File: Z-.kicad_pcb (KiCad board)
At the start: 4 copper layers, 98 x 98 mm, 147 parts, among them J1 200528-0100, J2 U.FL, J3 U.FL, J5 Conn_01x02, Q1 NX3008NBKS, Q10 MBT2222ADW1T1, Q11 NX3008NBKS, Q12 MBT2222ADW1T1, Q13 IRLML2803, Q14 SiRA99DP, Q15 IRFTS9342PBF, Q17 IRFTS9342PBF, Q19 IRFTS9342PBF, Q2 MBT2222ADW1T1, Q20 IRLML2803, Q21 SiRA99DP, Q3 NX3008NBKS, Q4 MBT2222ADW1T1, Q5 NX3008NBKS, Q6 MBT2222ADW1T1, Q7 NX3008NBKS, Q8 MBT2222ADW1T1, Q9 NX3008NBKS, U1 OPT4003DNPRQ1, U2 PCA9633DP2, U4 DRV8235RTER, U5 USBLC6-2P6

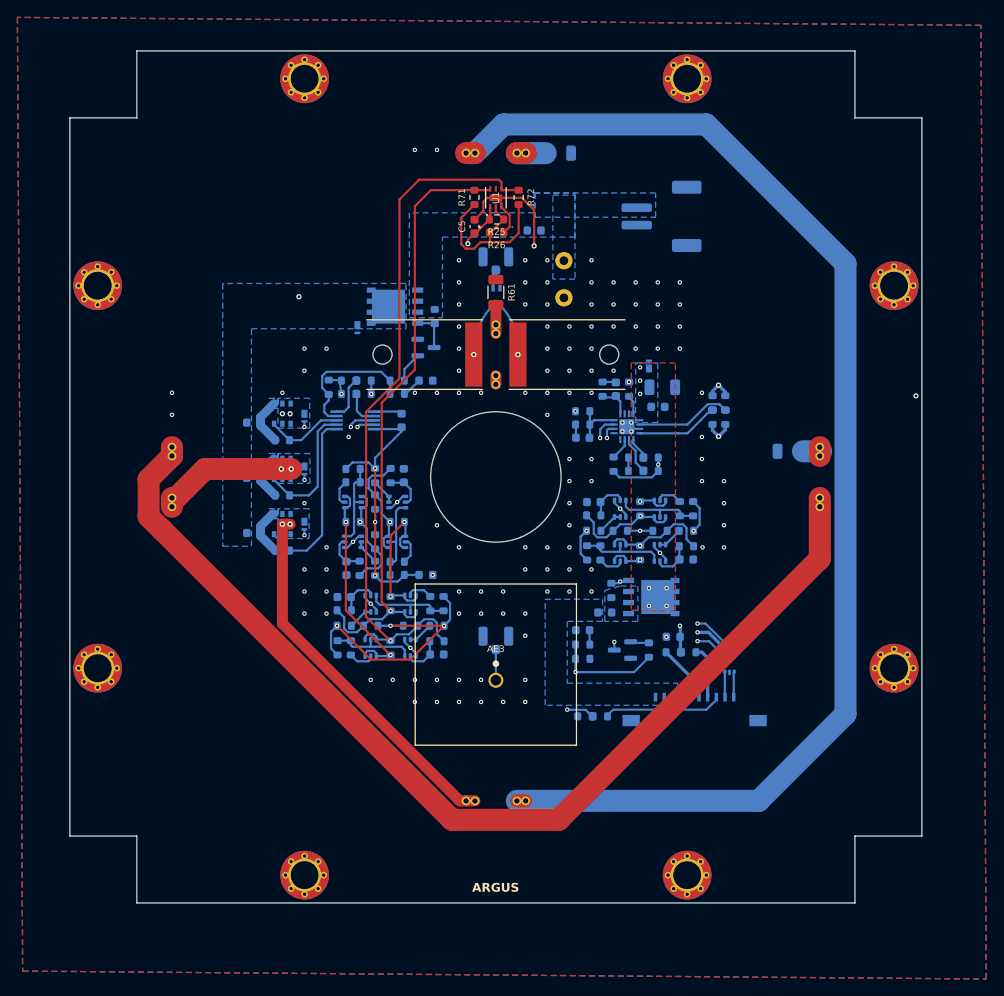
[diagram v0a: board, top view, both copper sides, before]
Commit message: Updated burnwire footprint and fuse specs
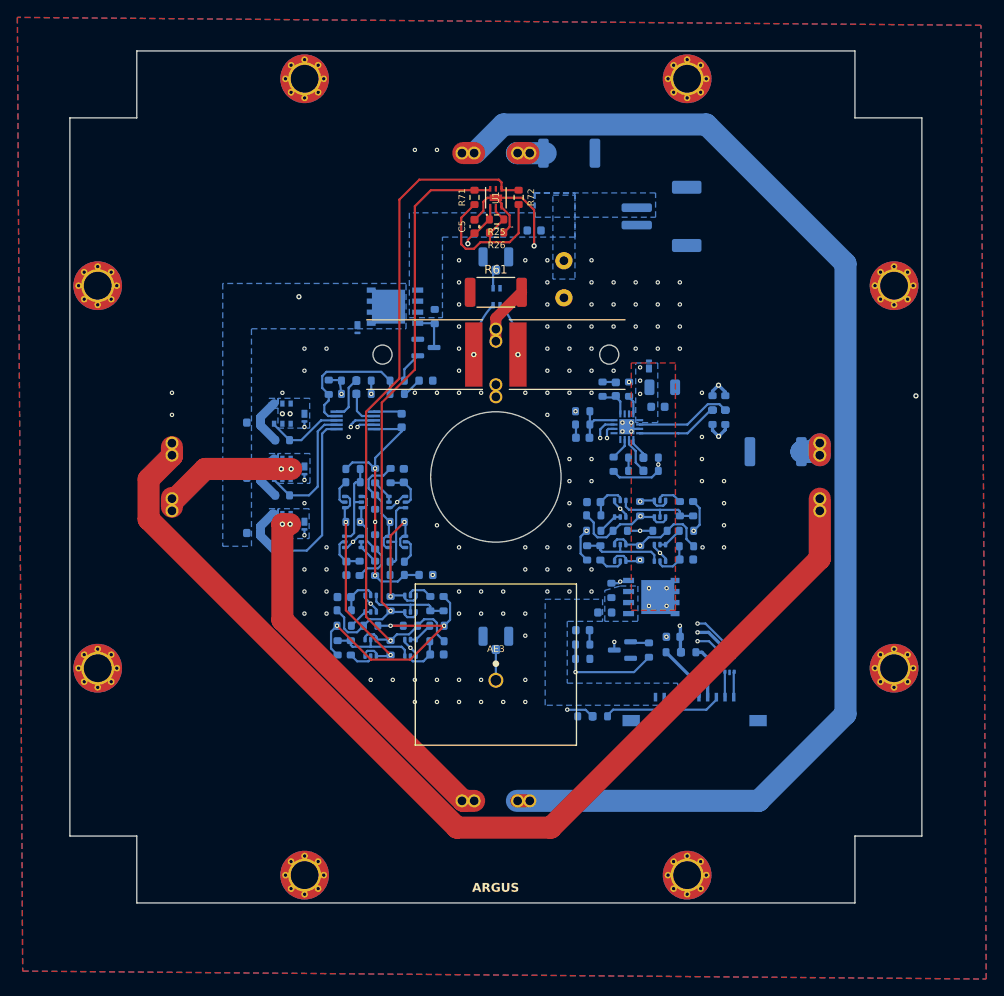
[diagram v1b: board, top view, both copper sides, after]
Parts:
- R43, R53, R60: value 100K -> 1k
- R44, R55, R61: footprint Resistor_SMD:R_1206_3216Metric -> Resistor_SMD:R_2512_6332Metric
- moved R44 1.68 mm to (184.5, 92.8)
- moved R55 1.24 mm to (160.8, 58.4)
- moved JP3 0.97 mm to (152.3, 82.5)
- turned R61 to 0 degrees
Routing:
- net Net-(JP3-B): track 3.29 -> 6.86 mm
- net Net-(JP4-B): track 3.11 -> 6.00 mm
- net /Burn Wires/VBURN3: track 28.1 -> 26.3 mm
- net Net-(JP1-B): track 120.2 -> 121.0 mm
- net /Burn Wires/VBURN2: track 42.9 -> 43.6 mm
- net GND: vias 130 -> 128

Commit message: Minor layout tweaks and gerbers exported
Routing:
- net GND: vias 128 -> 130
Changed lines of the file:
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@@
 			(drillshape 0)
 			(scaleselection 1)
-			(outputdirectory "../../../Gerbers/")
+			(outputdirectory "./Gerber")
 		)
 	)
@@
 			(pinfunction "MountPin")
 			(pintype "passive")
+			(zone_connect 1)
 		)
 		(pad "MP" smd rect
@@
 			(pinfunction "MountPin")
 			(pintype "passive")
+			(zone_connect 1)
 		)
 		(model "${KIPRJMOD}/../KiCad-Libraries/3D Models/2005280100.stp"
@@
 	)
 	(via
+		(at 172.72 117.856)
+		(size 0.508)
+		(drill 0.254)
+		(layers "F.Cu" "B.Cu")
+		(free yes)
+		(net 1)
+	)
+	(via
 		(at 163.322 106.299)
 		(size 0.508)
@@
 		(net 1)
 	)
+	(via
+		(at 172.212 118.618)
+		(size 0.508)
+		(drill 0.254)
+		(layers "F.Cu" "B.Cu")
+		(free yes)
+		(net 1)
+	)

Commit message: push
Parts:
- removed D8: GREEN, LED_SMD:LED_0603_1608Metric
- removed Q14: SiRA99DP, Argus-Miscellaneous:PowerPAK SO-8
- removed R73: 10k, Resistor_SMD:R_0603_1608Metric
- removed U5: USBLC6-2P6, Package_TO_SOT_SMD:SOT-666
- added D1: 10V, Diode_SMD:Nexperia_DSN1608-2_1.6x0.8mm, B.Cu at (154.7, 75.4)
- added F8: 1A, Fuse:Fuse_0603_1608Metric, B.Cu at (177.3, 73.2)
- added K1: G6B-1114P-US DC6, Argus-Miscellaneous:RELAY_G6B-1114P-US_OMR, B.Cu at (156.8, 73.2)
- added U3: USBLC6-2P6, Package_TO_SOT_SMD:SOT-666, B.Cu at (168.9, 118.4)
- AE1, AE2: footprint Argus-Miscellaneous:Antenna Mount -> Argus-Miscellaneous:Antenna Mount v2; moved to B.Cu
- D7: value 10V -> GREEN; footprint Diode_SMD:Nexperia_DSN1608-2_1.6x0.8mm -> LED_SMD:LED_0603_1608Metric
- F4, F5, F6: value 500mA -> 2A
- F7: value 2A -> 5A
- R61: moved to B.Cu
- moved R81 45.5 mm to (143.5, 82.5), turned to -90 degrees
- moved R80 43.0 mm to (143.5, 84.3), turned to 90 degrees
- moved R69 39.1 mm to (172.2, 86.9), turned to 180 degrees
- moved D5 36.5 mm to (147.8, 69.1), turned to 180 degrees
- moved F2 36.0 mm to (133.3, 72.6), turned to 90 degrees
- moved R53 35.8 mm to (147.8, 74.4)
- moved Q17 35.6 mm to (147.8, 71.6), turned to 180 degrees
- moved F5 34.9 mm to (147.8, 76.2), turned to 0 degrees
- moved D7 31.8 mm to (167.6, 84.3)
- moved R61 31.5 mm to (152.4, 105.9), turned to 90 degrees
- moved F4 30.4 mm to (151.9, 76.2), turned to 0 degrees
- moved R70 30.2 mm to (171.2, 84.3), turned to 90 degrees
- moved Q13 30.1 mm to (174.2, 84.3)
- moved R60 29.5 mm to (151.9, 74.4)
- moved Q19 29.4 mm to (151.9, 71.6), turned to 180 degrees
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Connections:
- D7 pad 1: /Burn Wires/VBURN_A_IN -> GND
- D7 pad 2: GND -> Net-(D7-A)
- F4 pad 2: /Burn Wires/VBURN_A_IN -> Net-(D1-K)
- F5 pad 2: /Burn Wires/VBURN_A_IN -> Net-(D1-K)
- F6 pad 2: /Burn Wires/VBURN_A_IN -> Net-(D1-K)
- R68 pad 2: Net-(D8-A) -> Net-(D7-A)
- U2 pad 1: BURN_EN2 -> BURN_EN1
- U2 pad 2: BURN_EN1 -> BURN_EN2
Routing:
- net Net-(JP2-B): track 146.6 -> 1.02 mm
- net Net-(JP1-B): track 121.0 -> 0.00 mm
- net LS_3V3: track 113.1 -> 16.0 mm, vias 5 -> 4
- net SDA: track 88.4 -> 11.8 mm, vias 4 -> 0
- net SCL: track 83.3 -> 11.8 mm, vias 4 -> 0
- net MAIN_3V3: track 84.7 -> 13.9 mm, vias 7 -> 3
- net SCL_LS: track 82.0 -> 12.5 mm, vias 1 -> 0
- net PERI_3V3: track 59.2 -> 0.00 mm, vias 3 -> 0
- net SDA_LS: track 70.9 -> 12.3 mm, vias 1 -> 0
- net /Burn Wires/VBURN2: track 43.6 -> 1.02 mm
- net /Burn Wires/VBURN3: track 26.3 -> 0.00 mm
- net BW_3V3: track 34.1 -> 10.8 mm
- net GND: track 47.9 -> 25.9 mm, vias 130 -> 9
- net BURN_RELAY_A: track 16.2 -> 35.5 mm, vias 0 -> 2
- net SCL_M: track 29.9 -> 11.8 mm, vias 2 -> 1
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- added copper zone on B.Cu, net Net-(D1-K)
- removed copper zone on B.Cu, net /Burn Wires/VBURN_A_IN
- removed copper zone on B.Cu, net /I2C Devices/VM
- removed copper zone on F.Cu, net /I2C Devices/VM
- removed copper zone on B.Cu, net GND
- removed copper zone on F.Cu, net GND
- removed copper zone on In1.Cu, net GND
- removed copper zone on In2.Cu, net GND
- removed copper zone on B.Cu, net Net-(F7-Pad1)
- removed copper zone on B.Cu, net Net-(Q21-S)
- removed copper zone on B.Cu, net VBATT
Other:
- outline, holes or cut-outs redrawn

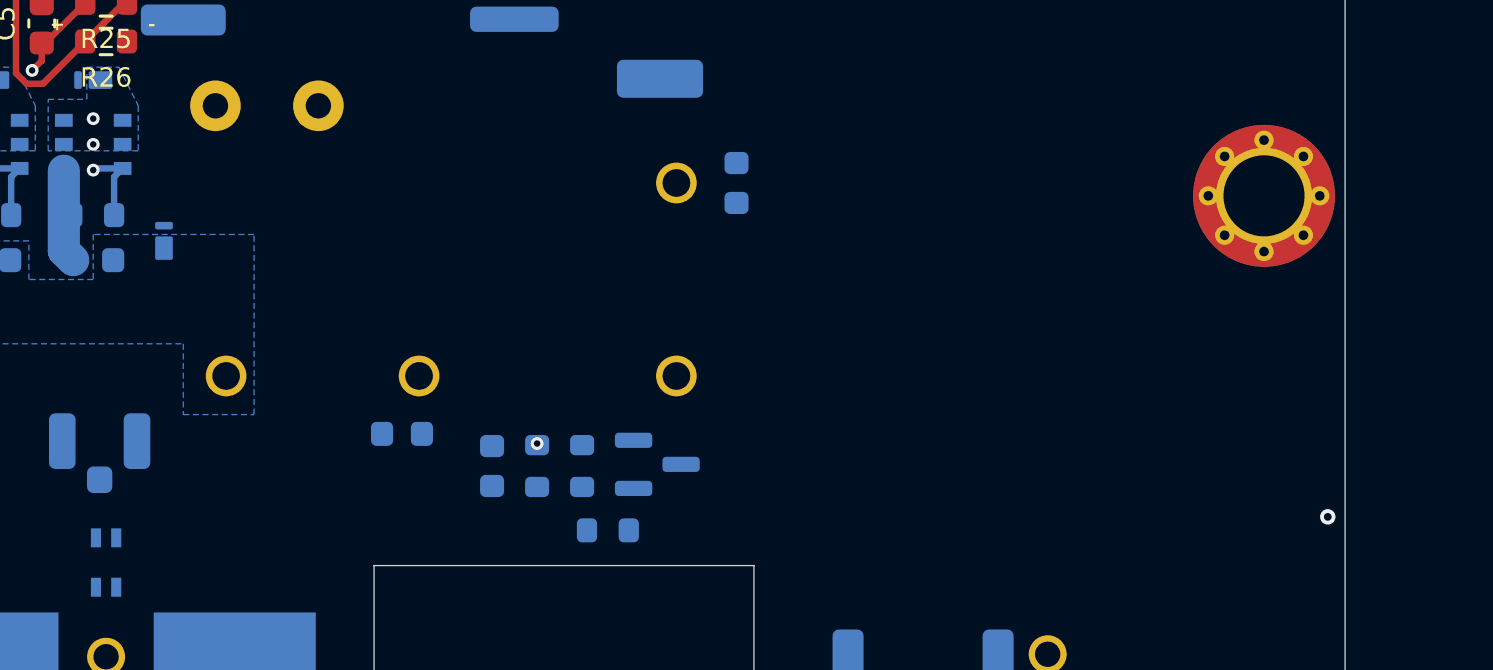
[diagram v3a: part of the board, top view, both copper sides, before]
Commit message: updated relay with old relay
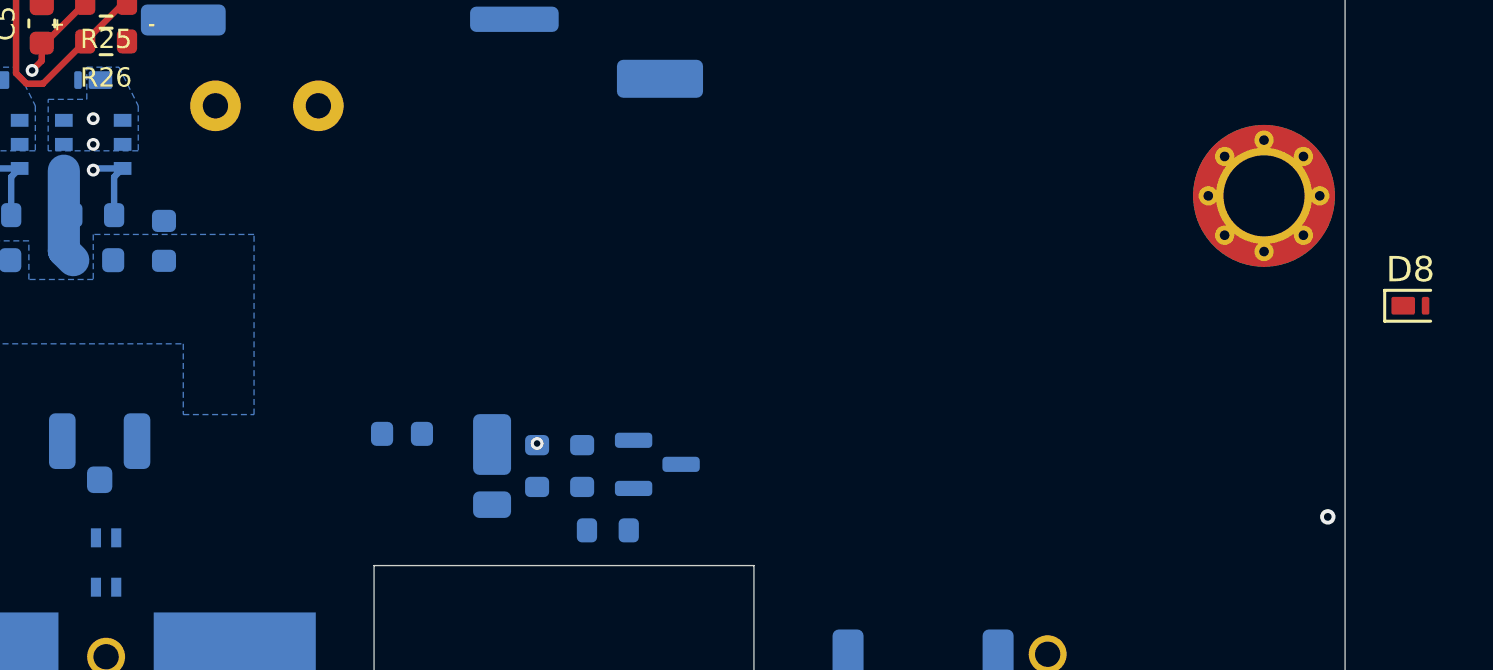
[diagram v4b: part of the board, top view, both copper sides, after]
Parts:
- removed F8: 1A, Fuse:Fuse_0603_1608Metric
- removed K1: G6B-1114P-US DC6, Argus-Miscellaneous:RELAY_G6B-1114P-US_OMR
- added D8: 10V, Diode_SMD:Nexperia_DSN1608-2_1.6x0.8mm, F.Cu at (203.9, 78.0)
- D1: value 10V -> GREEN; footprint Diode_SMD:Nexperia_DSN1608-2_1.6x0.8mm -> LED_SMD:LED_0603_1608Metric
- D7: value GREEN -> DFLS130L; footprint LED_SMD:LED_0603_1608Metric -> Diode_SMD:D_PowerDI-123
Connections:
- D1 pad 1: Net-(D1-K) -> GND
- D1 pad 2: GND -> Net-(D1-A)
- D7 pad 1: GND -> Net-(D7-K)
- F4 pad 2: Net-(D1-K) -> /Burn Wires/VBURN_A_IN
- F5 pad 2: Net-(D1-K) -> /Burn Wires/VBURN_A_IN
- F6 pad 2: Net-(D1-K) -> /Burn Wires/VBURN_A_IN
- F7 pad 1: Net-(F7-Pad1) -> Net-(D7-K)
- Q13 pad 3: Net-(Q13-D) -> Net-(D7-A)
- R68 pad 2: Net-(D7-A) -> Net-(D1-A)
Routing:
- added copper zone on B.Cu, net /Burn Wires/VBURN_A_IN
- removed copper zone on B.Cu, net Net-(D1-K)

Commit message: Updated PCB
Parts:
- added K1: IM02, Argus-Miscellaneous:RELAY8_SMTGUL_TEC, B.Cu at (163.3, 79.0)
- D8: moved to B.Cu
- moved JP2 74.5 mm to (152.4, 58.4)
- moved JP5 74.4 mm to (152.4, 132.8), turned to -90 degrees
- moved R55 64.1 mm to (149.1, 127.5), turned to -90 degrees
- moved D8 43.6 mm to (160.8, 84.3), turned to 180 degrees
- moved R80 34.7 mm to (146.3, 118.9)
- moved R81 34.7 mm to (146.3, 117.1)
- moved D1 20.7 mm to (174.2, 82.3), turned to 180 degrees
- moved D7 11.7 mm to (165.4, 72.9), turned to 0 degrees
- moved F7 10.7 mm to (160.8, 72.9)
- moved R69 8.38 mm to (174.2, 78.7), turned to -90 degrees
- moved Q13 8.20 mm to (171.4, 76.5), turned to 90 degrees
- moved R70 4.32 mm to (171.2, 80.0), turned to 180 degrees
- moved R68 2.70 mm to (171.2, 82.3), turned to 0 degrees
- moved F3 1.80 mm to (146.3, 113.8), turned to 90 degrees
- moved H10 1.52 mm to (162.3, 70.1)
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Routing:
- net Net-(JP2-B): track 1.02 -> 116.3 mm
- net Net-(JP1-B): track 0.00 -> 88.7 mm
- net SDA: track 11.8 -> 98.9 mm, vias 0 -> 4
- net SCL: track 11.8 -> 89.2 mm, vias 0 -> 4
- net MAIN_3V3: track 13.9 -> 79.0 mm, vias 3 -> 8
- net SCL_LS: track 12.5 -> 75.5 mm, vias 0 -> 2
- net LS_3V3: track 16.0 -> 78.1 mm
- net SDA_LS: track 12.3 -> 74.1 mm, vias 0 -> 2
- net PERI_3V3: track 0.00 -> 54.7 mm, vias 0 -> 3
- net /Burn Wires/VBURN1: track 0.00 -> 43.0 mm
- net /PERI_3V3_OR_GND: track 1.93 -> 32.4 mm, vias 1 -> 2
- net /Burn Wires/VBURN3: track 0.00 -> 26.3 mm
- net BW_3V3: track 10.8 -> 35.7 mm, vias 3 -> 5
- net /coil: track 23610.9 -> 23629.3 mm
- net /Burn Wires/VBURN2: track 1.02 -> 16.2 mm
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- added copper zone on B.Cu, net /I2C Devices/VM
- added copper zone on B.Cu, net GND
- added copper zone on F.Cu, net GND
- added copper zone on In1.Cu, net GND
- added copper zone on In2.Cu, net GND
- added copper zone on B.Cu, net Net-(D7-K)
- added copper zone on B.Cu, net VBATT

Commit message: Done, still needs silkscreen
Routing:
- net GND: track 27.3 -> 22.0 mm, vias 10 -> 106

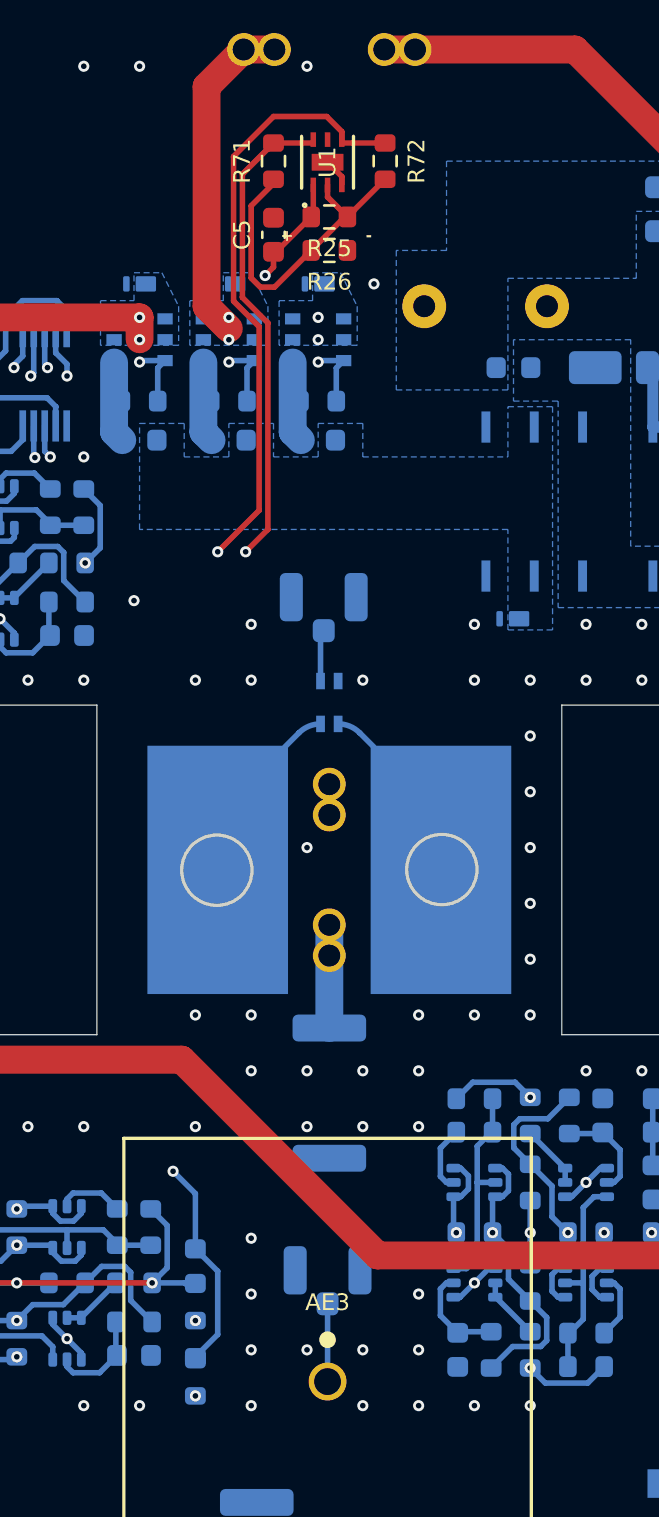
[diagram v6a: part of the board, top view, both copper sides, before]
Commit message: Updated silkscreen and gps/antenna parameters for 50ohm
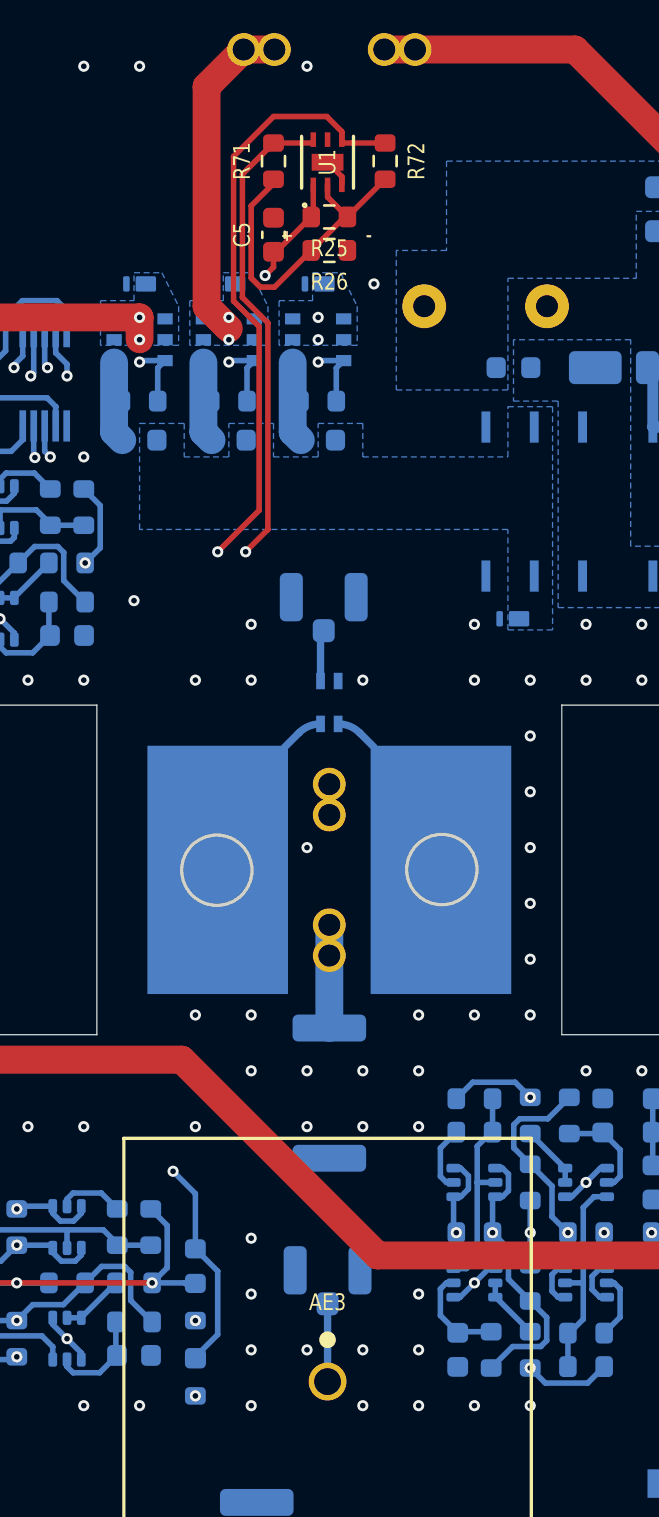
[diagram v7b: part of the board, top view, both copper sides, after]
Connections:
- net Net-(AE3-A) renamed /GPS
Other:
- board text added: "ARGUS Cubesat Carnegie Mellon University Z- Solar Panel v4"
- board text removed: "ARGUS Cubesat Carnegie Mellon University Z- Solar Panel v3"
